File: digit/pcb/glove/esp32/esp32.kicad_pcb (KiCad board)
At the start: 2 copper layers, 91.4 x 63.5 mm, 68 parts, among them IC1 MDBT53-P1M, IC2 LTC3119EFE#PBF, IC3 DRV2605LDGSR, IC4 DRV2605LDGSR, IC5 TCA9546ADR, J1 Conn_02x05_Odd_Even, J10 Conn_01x03_Pin, J11 Conn_01x02_Pin, J12 Conn_01x02_Pin, J13 Conn_01x05_Pin, J14 Conn_01x02_Pin, J15 Conn_01x01_Pin, J16 Conn_01x02_Pin, J2 Conn_01x02_Pin, J3 Conn_01x02_Pin, J4 Conn_01x02_Pin, J5 Conn_01x02_Pin, J6 Conn_01x02_Pin, J7 Conn_01x02_Pin, J8 Conn_01x02_Pin, J9 Conn_01x02_Pin, Y1 FC-135R_32.7680KA-AG0

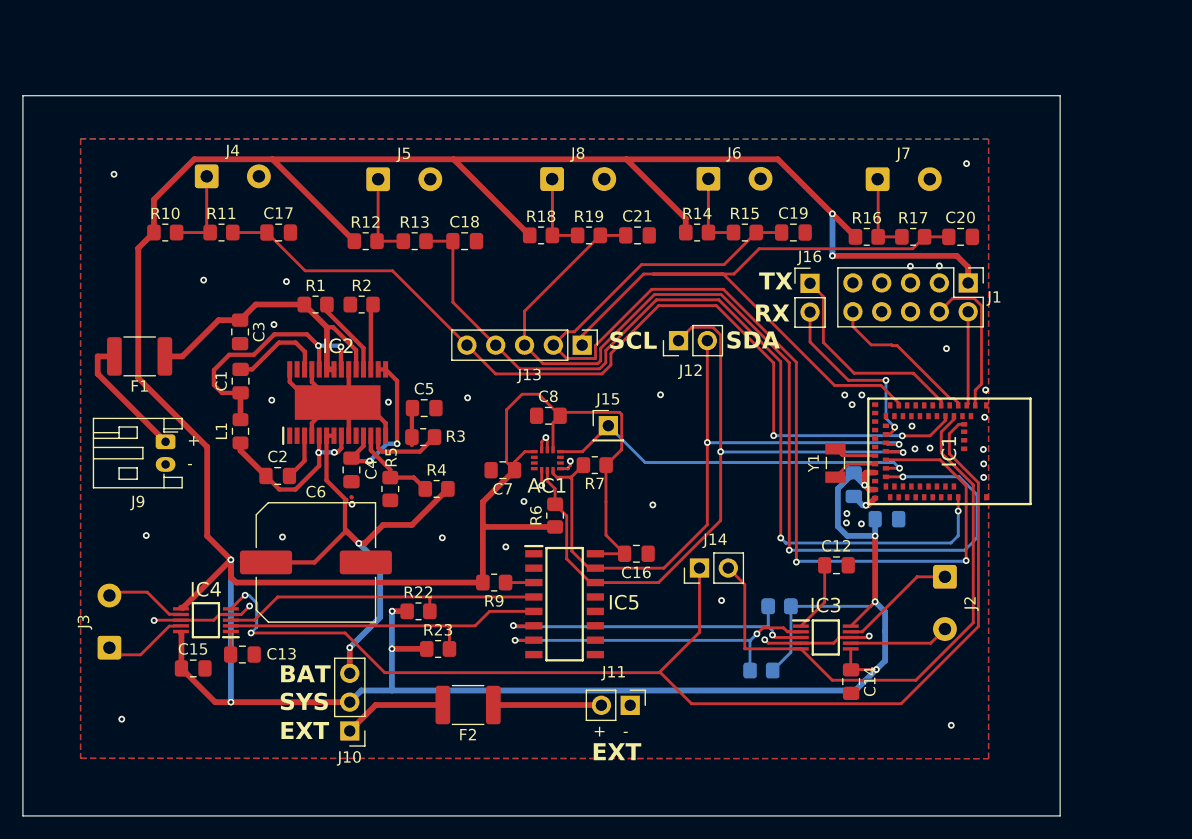
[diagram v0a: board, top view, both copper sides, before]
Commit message: Changed directory names to be proper
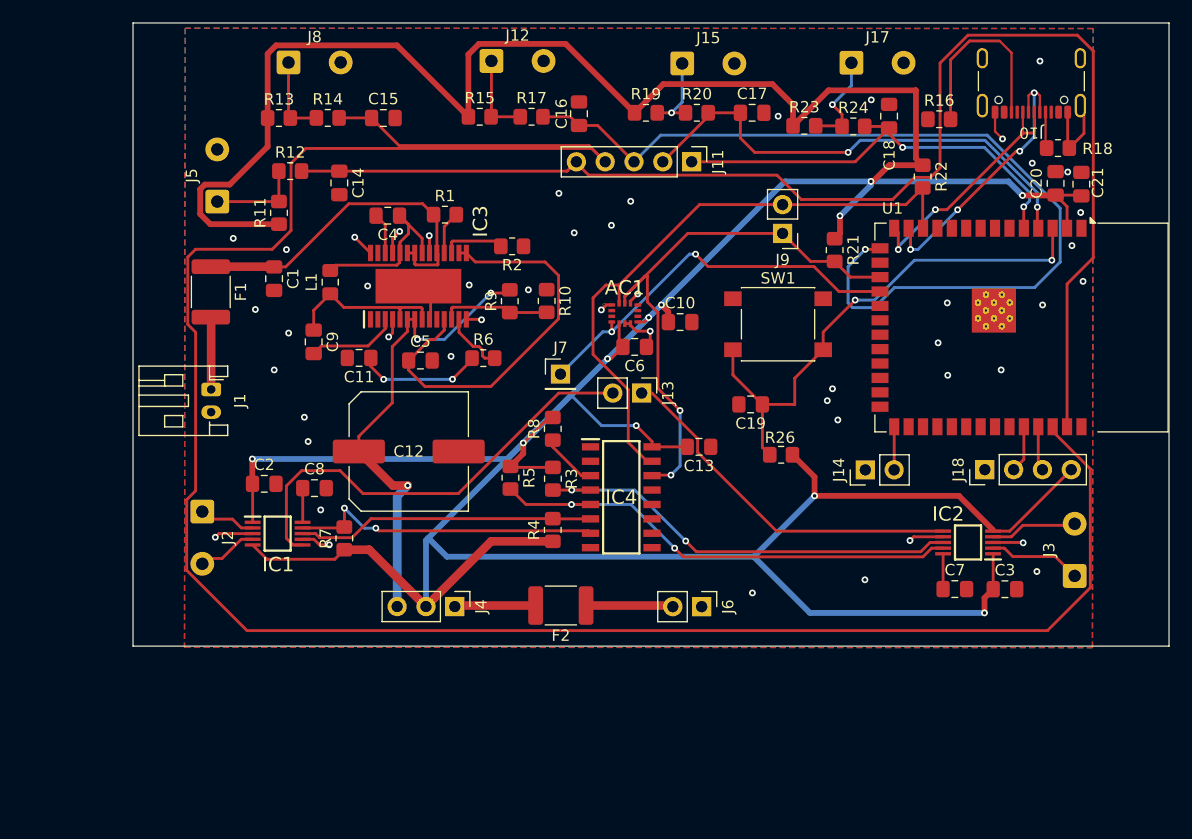
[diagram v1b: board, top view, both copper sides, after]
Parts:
- removed IC5: TCA9546ADR, TCA9546ADR:SOIC127P600X175-16N
- removed J16: Conn_01x02_Pin, Connector_PinHeader_2.54mm:PinHeader_1x02_P2.54mm_Vertical
- removed Y1: FC-135R_32.7680KA-AG0, FC-135R_32.768KA-AGO:XTAL_FC-135R_32.7680KA-AG0
- added C11: 470pF, Capacitor_SMD:C_0805_2012Metric_Pad1.18x1.45mm_HandSolder, F.Cu at (121.1, 91.7)
- added J17: Conn_01x02_Pin, Connector_Wire:SolderWire-0.5sqmm_1x02_P4.6mm_D0.9mm_OD2.1mm, F.Cu at (164.5, 65.7)
- added J18: Conn_01x04_Pin, Connector_PinHeader_2.54mm:PinHeader_1x04_P2.54mm_Vertical, F.Cu at (176.2, 101.5)
- added R24: 1k, Resistor_SMD:R_0805_2012Metric_Pad1.20x1.40mm_HandSolder, F.Cu at (164.7, 71.3)
- added R26: 10k, Resistor_SMD:R_0805_2012Metric_Pad1.20x1.40mm_HandSolder, F.Cu at (158.3, 100.2)
- added R8: 10k, Resistor_SMD:R_0805_2012Metric_Pad1.20x1.40mm_HandSolder, F.Cu at (138.2, 98.0)
- added SW1: SW_Push, Button_Switch_SMD:SW_SPST_PTS645, F.Cu at (158.0, 88.7)
- added U1: ESP32-S3-WROOM-1, RF_Module:ESP32-S3-WROOM-1, F.Cu at (179.5, 89.0)
- C1: value 0.1µF -> 10µF
- C10: value 4.7µF -> 100nF; moved to F.Cu
- C12: value 1µF -> 150µF; footprint Capacitor_SMD:C_0805_2012Metric_Pad1.18x1.45mm_HandSolder -> Capacitor_SMD:C_Elec_10x10.2
- C13: value 1µF -> 0.1µF
- C14, C15: value 1µF -> 100nF
- C16: value 0.1µF -> 100nF
- C19, C20: value 100nF -> 0.1uF
- C2: value 0.1µF -> 1µF
- C21: value 100nF -> 22uF
- C3: value 10µF -> 1µF
- C4: value 4.7µF -> 0.1µF
- C5: value 470pF -> 4.7µF
- C6: value 150µF -> 100nF; footprint Capacitor_SMD:C_Elec_10x10.2 -> Capacitor_SMD:C_0805_2012Metric_Pad1.18x1.45mm_HandSolder
- C7, C8: value 100nF -> 1µF
- C9: value 2.2µF -> 0.1µF; moved to F.Cu
- IC1: value MDBT53-P1M -> DRV2605LDGSR; footprint MDBT53-P1M:MDBT53P1M -> DRV2605LDGSR:SOP50P490X110-10N
- IC2: value LTC3119EFE#PBF -> DRV2605LDGSR; footprint LTC3119EFE#PBF:SOP65P640X120-29N -> DRV2605LDGSR:SOP50P490X110-10N
- IC3: value DRV2605LDGSR -> LTC3119EFE#PBF; footprint DRV2605LDGSR:SOP50P490X110-10N -> LTC3119EFE#PBF:SOP65P640X120-29N
- IC4: value DRV2605LDGSR -> TCA9546ADR; footprint DRV2605LDGSR:SOP50P490X110-10N -> TCA9546ADR:SOIC127P600X175-16N
- J1: value Conn_02x05_Odd_Even -> Conn_01x02_Pin; footprint Connector_PinHeader_2.54mm:PinHeader_2x05_P2.54mm_Vertical -> Connector_JST:JST_PH_S2B-PH-K_1x02_P2.00mm_Horizontal
- J10: value Conn_01x03_Pin -> USB_C_Receptacle_USB2.0_16P; footprint Connector_PinHeader_2.54mm:PinHeader_1x03_P2.54mm_Vertical -> Connector_USB:USB_C_Receptacle_GCT_USB4105-xx-A_16P_TopMnt_Horizontal
- J11: value Conn_01x02_Pin -> Conn_01x05_Pin; footprint Connector_PinHeader_2.54mm:PinHeader_1x02_P2.54mm_Vertical -> Connector_PinHeader_2.54mm:PinHeader_1x05_P2.54mm_Vertical
- J12: footprint Connector_PinHeader_2.54mm:PinHeader_1x02_P2.54mm_Vertical -> Connector_Wire:SolderWire-0.5sqmm_1x02_P4.6mm_D0.9mm_OD2.1mm
- J13: value Conn_01x05_Pin -> Conn_01x02_Pin; footprint Connector_PinHeader_2.54mm:PinHeader_1x05_P2.54mm_Vertical -> Connector_PinHeader_2.54mm:PinHeader_1x02_P2.54mm_Vertical
- J15: value Conn_01x01_Pin -> Conn_01x02_Pin; footprint Connector_PinHeader_2.54mm:PinHeader_1x01_P2.54mm_Vertical -> Connector_Wire:SolderWire-0.5sqmm_1x02_P4.6mm_D0.9mm_OD2.1mm
- J4: value Conn_01x02_Pin -> Conn_01x03_Pin; footprint Connector_Wire:SolderWire-0.5sqmm_1x02_P4.6mm_D0.9mm_OD2.1mm -> Connector_PinHeader_2.54mm:PinHeader_1x03_P2.54mm_Vertical
- J6: footprint Connector_Wire:SolderWire-0.5sqmm_1x02_P4.6mm_D0.9mm_OD2.1mm -> Connector_PinHeader_2.54mm:PinHeader_1x02_P2.54mm_Vertical
- J7: value Conn_01x02_Pin -> Conn_01x01_Pin; footprint Connector_Wire:SolderWire-0.5sqmm_1x02_P4.6mm_D0.9mm_OD2.1mm -> Connector_PinHeader_2.54mm:PinHeader_1x01_P2.54mm_Vertical
- J9: footprint Connector_JST:JST_PH_S2B-PH-K_1x02_P2.00mm_Horizontal -> Connector_PinHeader_2.54mm:PinHeader_1x02_P2.54mm_Vertical
- R10: value 22k -> 100k
- R11, R13, R15, R19: value 1k -> 22k
- R12, R14: value 22k -> 1k
- R16, R18: value 22k -> 5.1k
- R20: value 10k -> 1k; moved to F.Cu
- R21: moved to F.Cu
- R23: value 10k -> 22k
- R3: value 52.3k -> 10k
- R4: value 316k -> 10k
- R5: value 100k -> 10k
- R6: value 10k -> 52.3k
- R9: value 10k -> 316k
- moved J3 85.3 mm to (184.2, 110.9)
- moved J10 83.7 mm to (180.3, 66.4)
- moved C3 71.1 mm to (178.0, 112.1), turned to 0 degrees
- moved J1 67.4 mm to (108.0, 94.5)
- moved J2 65.7 mm to (107.2, 105.2)
- moved C14 63.0 mm to (119.3, 76.3)
- moved IC1 59.7 mm to (113.9, 107.2), turned to 0 degrees
- moved R22 58.7 mm to (170.8, 75.7), turned to -90 degrees
- moved J9 57.4 mm to (158.4, 80.7), turned to 180 degrees
- moved IC2 56.9 mm to (174.8, 108.0), turned to 180 degrees
- moved R23 56.3 mm to (160.3, 71.2)
- moved C15 51.3 mm to (123.2, 70.5)
- moved R20 49.5 mm to (150.8, 70.1), turned to 0 degrees
- moved C9 49.3 mm to (117.1, 90.3)
- moved J11 48.2 mm to (150.4, 74.4)
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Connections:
- C1 pad 1: Net-(IC2-SW1_1) -> Net-(IC3-PVIN_1)
- C1 pad 2: Net-(IC2-BST1) -> GND
- C12 pad 1: Net-(IC3-REG) -> /BB_3V3
- C13 pad 1: Net-(IC4-REG) -> GND
- C13 pad 2: GND -> SYS_3V3
- C14 pad 1: SYS_3V3 -> /FLEX1_ADC
- C15 pad 1: SYS_3V3 -> /FLEX2_ADC
- C16 pad 1: GND -> /FLEX3_ADC
- C16 pad 2: SYS_3V3 -> GND
- C17 pad 1: /FLEX1_ADC -> /FLEX4_ADC
- C18 pad 1: /FLEX2_ADC -> /FLEX5_ADC
- C19 pad 1: /FLEX4_ADC -> /EN
- C2 pad 1: Net-(IC2-SW2_1) -> SYS_3V3
- C2 pad 2: Net-(IC2-BST2) -> GND
- C20 pad 1: /FLEX5_ADC -> SYS_3V3
- C21 pad 1: /FLEX3_ADC -> SYS_3V3
- C3 pad 1: Net-(IC2-PVIN_1) -> SYS_3V3
- C4 pad 1: Net-(IC2-MPPC) -> Net-(IC3-SW1_1)
- C4 pad 2: GND -> Net-(IC3-BST1)
- C5 pad 1: Net-(C5-Pad1) -> Net-(IC3-MPPC)
- C6 pad 1: /BB_3V3 -> GND
- C6 pad 2: GND -> SYS_3V3
- C7 pad 1: SYS_3V3 -> Net-(IC2-VDD)
- C8 pad 1: GND -> Net-(IC1-VDD)
- C8 pad 2: SYS_3V3 -> GND
- C9 pad 1: SYS_3V3 -> Net-(IC3-SW2_1)
- C9 pad 2: GND -> Net-(IC3-BST2)
- F1 pad 1: Net-(IC2-PVIN_1) -> Net-(IC3-PVIN_1)
- F2 pad 2: Net-(J10-Pin_1) -> Net-(J4-Pin_1)
- IC1 pad 1: GND -> SYS_3V3
- IC1 pad 10: /UART_TX -> Net-(IC1-VDD)
- IC1 pad 2: /SWDCLK -> Net-(IC1-SCL)
- IC1 pad 3: unconnected-(IC1-P1.08-Pad3) -> GND
- IC1 pad 4: /SWDIO -> Net-(IC1-IN/TRIG)
- IC1 pad 5: unconnected-(IC1-P0.27-Pad5) -> SYS_3V3
- IC1 pad 6: /RESET -> /HAPTIC_DRIVER1_EN
- IC1 pad 7: /HAPTIC_DRIVER1_EN -> GND
- IC1 pad 8: unconnected-(IC1-P0.24-Pad8) -> Net-(IC1-GND)
- IC1 pad 9: /FLEX1_ADC -> Net-(IC1-OUT-)
- IC2 pad 1: unconnected-(IC2-N/C_1-Pad1) -> SYS_3V3
- IC2 pad 10: unconnected-(IC2-PGOOD-Pad10) -> Net-(IC2-VDD)
- IC2 pad 2: unconnected-(IC2-N/C_2-Pad2) -> Net-(IC2-SCL)
- IC2 pad 3: Net-(IC2-BST2) -> GND
- IC2 pad 4: GND -> Net-(IC2-IN/TRIG)
- IC2 pad 5: Net-(IC2-SW2_1) -> SYS_3V3
- IC2 pad 6: /BB_3V3 -> /HAPTIC_DRIVER2_EN
- IC2 pad 7: /BB_3V3 -> GND
- IC2 pad 8: Net-(IC2-SW2_1) -> Net-(IC2-GND)
- IC2 pad 9: GND -> Net-(IC2-OUT-)
- IC3 pad 1: Net-(IC3-REG) -> unconnected-(IC3-N/C_1-Pad1)
- IC3 pad 10: SYS_3V3 -> unconnected-(IC3-PGOOD-Pad10)
- IC3 pad 2: Net-(IC3-SCL) -> unconnected-(IC3-N/C_2-Pad2)
- IC3 pad 3: Net-(IC3-SDA) -> Net-(IC3-BST2)
- IC3 pad 5: /HAPTIC_DRIVER1_EN -> Net-(IC3-SW2_1)
- IC3 pad 6: SYS_3V3 -> /BB_3V3
- IC3 pad 7: Net-(IC3-OUT+) -> /BB_3V3
- IC3 pad 8: GND -> Net-(IC3-SW2_1)
- IC3 pad 9: Net-(IC3-OUT-) -> GND
- IC4 pad 1: Net-(IC4-REG) -> GND
- IC4 pad 10: SYS_3V3 -> unconnected-(IC4-SC2-Pad10)
- IC4 pad 2: Net-(IC4-SCL) -> GND
- IC4 pad 3: Net-(IC4-SDA) -> Net-(IC4-~{RESET})
- IC4 pad 4: GND -> Net-(IC2-GND)
- IC4 pad 5: /HAPTIC_DRIVER2_EN -> Net-(IC2-OUT-)
- IC4 pad 6: SYS_3V3 -> Net-(IC1-GND)
- IC4 pad 7: Net-(IC4-OUT+) -> Net-(IC1-OUT-)
- IC4 pad 9: Net-(IC4-OUT-) -> unconnected-(IC4-SD2-Pad9)
- J1 pad 1: SYS_3V3 -> +3.7V
- J1 pad 2: /SWDIO -> GND
- J11 pad 1: GND -> /FLEX5_ADC
- J11 pad 2: /EXT_3V3 -> /FLEX4_ADC
- J12 pad 1: /I2C_SCL -> Net-(J12-Pin_1)
- J12 pad 2: /I2C_SDA -> GND
- J13 pad 1: /FLEX5_ADC -> /HAPTIC_DRIVER2_EN
- J13 pad 2: /FLEX4_ADC -> /HAPTIC_DRIVER1_EN
- J14 pad 1: /HAPTIC_DRIVER2_EN -> GND
- J14 pad 2: /HAPTIC_DRIVER1_EN -> /BOOT
- J15 pad 1: /IMU_INT1 -> Net-(J15-Pin_1)
- J2 pad 1: Net-(IC3-OUT-) -> Net-(IC1-SCL)
- J2 pad 2: Net-(IC3-OUT+) -> Net-(IC1-IN/TRIG)
- J3 pad 1: Net-(IC4-OUT-) -> Net-(IC2-SCL)
- J3 pad 2: Net-(IC4-OUT+) -> Net-(IC2-IN/TRIG)
- J4 pad 2: GND -> SYS_3V3
- J6 pad 1: Net-(J6-Pin_1) -> GND
- J6 pad 2: GND -> /EXT_3V3
- J7 pad 1: Net-(J7-Pin_1) -> /IMU_INT1
- J9 pad 1: +3.7V -> /I2C_SCL
- J9 pad 2: GND -> /I2C_SDA
- L1 pad 1: Net-(IC2-SW2_1) -> Net-(IC3-SW2_1)
- L1 pad 2: Net-(IC2-SW1_1) -> Net-(IC3-SW1_1)
- R1 pad 1: Net-(IC2-PVIN_1) -> Net-(IC3-PVIN_1)
- R1 pad 2: Net-(IC2-RUN) -> Net-(IC3-RUN)
- R10 pad 1: SYS_3V3 -> GND
- R10 pad 2: Net-(J4-Pin_1) -> Net-(IC3-FB)
- R11 pad 1: Net-(J4-Pin_1) -> SYS_3V3
- R11 pad 2: /FLEX1_ADC -> Net-(J5-Pin_1)
- R12 pad 1: SYS_3V3 -> Net-(J5-Pin_1)
- R12 pad 2: Net-(J5-Pin_1) -> /FLEX1_ADC
- R13 pad 1: Net-(J5-Pin_1) -> SYS_3V3
- R13 pad 2: /FLEX2_ADC -> Net-(J8-Pin_1)
- R14 pad 1: SYS_3V3 -> Net-(J8-Pin_1)
- R14 pad 2: Net-(J6-Pin_1) -> /FLEX2_ADC
- R15 pad 1: Net-(J6-Pin_1) -> SYS_3V3
- R15 pad 2: /FLEX4_ADC -> Net-(J12-Pin_1)
- R16 pad 1: SYS_3V3 -> GND
- R16 pad 2: Net-(J7-Pin_1) -> Net-(J10-CC2)
- R17 pad 1: Net-(J7-Pin_1) -> Net-(J12-Pin_1)
- R17 pad 2: /FLEX5_ADC -> /FLEX3_ADC
- R18 pad 1: SYS_3V3 -> GND
- R18 pad 2: Net-(J8-Pin_1) -> Net-(J10-CC1)
- R19 pad 1: Net-(J8-Pin_1) -> SYS_3V3
- R19 pad 2: /FLEX3_ADC -> Net-(J15-Pin_1)
- R2 pad 2: Net-(IC2-RT) -> Net-(IC3-RT)
- R20 pad 1: SYS_3V3 -> Net-(J15-Pin_1)
- R20 pad 2: Net-(IC3-SCL) -> /FLEX4_ADC
- R21 pad 2: Net-(IC3-SDA) -> /I2C_SCL
- R22 pad 2: Net-(IC4-SDA) -> /I2C_SDA
- R23 pad 2: Net-(IC4-SCL) -> Net-(J17-Pin_1)
- R3 pad 1: Net-(C5-Pad1) -> SYS_3V3
- R3 pad 2: Net-(IC2-VC) -> Net-(IC2-GND)
- R4 pad 1: Net-(IC2-FB) -> SYS_3V3
- R4 pad 2: /BB_3V3 -> Net-(IC1-GND)
- R5 pad 1: GND -> SYS_3V3
- R5 pad 2: Net-(IC2-FB) -> Net-(IC2-OUT-)
- R6 pad 1: SYS_3V3 -> Net-(C11-Pad1)
- R6 pad 2: /I2C_SCL -> Net-(IC3-VC)
- R7 pad 2: /I2C_SDA -> Net-(IC1-OUT-)
- R9 pad 1: Net-(IC5-~{RESET}) -> Net-(IC3-FB)
- R9 pad 2: SYS_3V3 -> /BB_3V3
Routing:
- net /FLEX2_ADC: track 79.6 -> 197.0 mm, vias 2 -> 0
- net /HAPTIC_DRIVER2_EN: track 105.8 -> 32.3 mm, vias 2 -> 0
- net /FLEX4_ADC: track 99.3 -> 43.3 mm
- net /EN: track 0.00 -> 46.5 mm, vias 0 -> 2
- net Net-(IC2-OUT-): track 0.00 -> 42.6 mm, vias 0 -> 2
- net Net-(IC2-GND): track 0.00 -> 38.6 mm, vias 0 -> 2
- net /FLEX1_ADC: track 80.5 -> 117.6 mm, vias 2 -> 0
- net Net-(IC3-MPPC): track 0.00 -> 35.8 mm
- net Net-(IC3-PVIN_1): track 0.00 -> 30.6 mm
- net Net-(IC3-SCL): track 30.1 -> 0.00 mm, vias 2 -> 0
- net Net-(IC3-SDA): track 29.6 -> 0.00 mm, vias 2 -> 0
- net Net-(IC4-SCL): track 29.3 -> 0.00 mm
- net Net-(IC4-SDA): track 28.9 -> 0.00 mm
- net Net-(IC1-OUT-): track 0.00 -> 28.0 mm, vias 0 -> 2
- net Net-(IC2-PVIN_1): track 26.4 -> 0.00 mm
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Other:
- board size 91.4 x 63.5 mm -> 91.3 x 54.9 mm
- board text removed: "+"
- board text removed: "-"
- board text removed: "BAT"
- board text removed: "EXT"
- board text removed: "RX"
- board text removed: "SCL"
- board text removed: "SDA"
- board text removed: "SYS"
- board text removed: "TX"
